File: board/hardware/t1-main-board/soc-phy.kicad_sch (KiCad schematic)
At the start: 1 part, among them U1301 RK3566

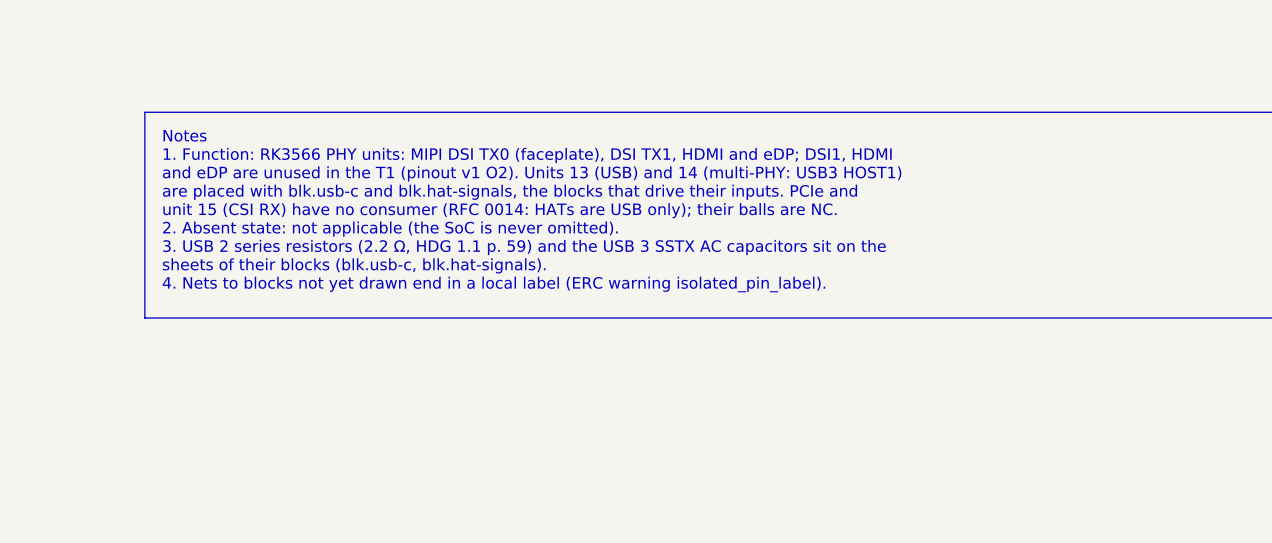
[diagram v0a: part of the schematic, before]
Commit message: Board: capture blk.maskrom
Power + Vol- at a cold power-on pull eMMC D0 low inside the TPS3808G01
boot window (BOM v1 lines 35, 78, 97, 98; sim/maskrom): SENSE 280k/100k,
CT 390 nF, WINDOW_N with its pad, SN74LVC1G57 and SN74LVC1G58 on
vcca1v8_pmu, BAT54 from PWRON_N, DMG1012T through 1 kΩ to EMMC_D0.
Every block in use now has its sheet; the README states the remaining
single-pin nets.

Co-Authored-By: Claude Opus 5.5 <noreply@anthropic.com>
Claude-Session: https://claude.ai/code/session_01Ei262h3TpgY9vyfNLMi5Mn
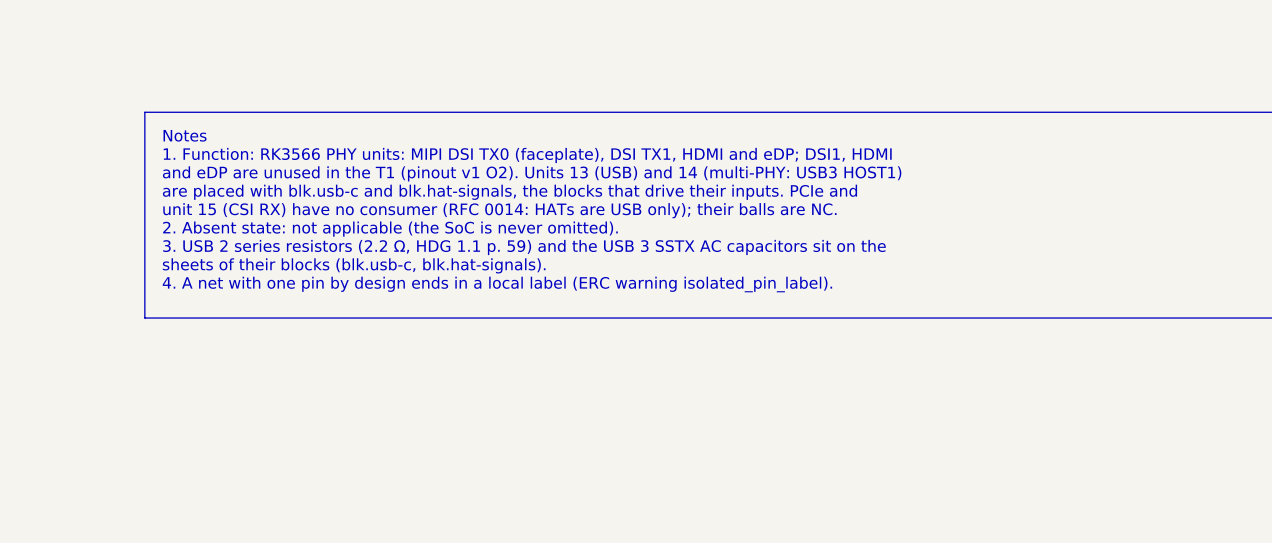
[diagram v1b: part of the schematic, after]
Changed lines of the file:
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@@
 (no_connect (at 76.2 138.43))
 (no_connect (at 76.2 140.97))
-(text_box "Notes\n1. Function: RK3566 PHY units: MIPI DSI TX0 (faceplate), DSI TX1, HDMI and eDP; DSI1, HDMI\n   and eDP are unused in the T1 (pinout v1 O2). Units 13 (USB) and 14 (multi-PHY: USB3 HOST1)\n   are placed with blk.usb-c and blk.hat-signals, the blocks that drive their inputs. PCIe and\n   unit 15 (CSI RX) have no consumer (RFC 0014: HATs are USB only); their balls are NC.\n2. Absent state: not applicable (the SoC is never omitted).\n3. USB 2 series resistors (2.2 Ω, HDG 1.1 p. 59) and the USB 3 SSTX AC capacitors sit on the\n   sheets of their blocks (blk.usb-c, blk.hat-signals).\n4. Nets to blocks not yet drawn end in a local label (ERC warning isolated_pin_label)." (exclude_from_sim no) (at 275.59 226.06 0) (size 129.54 22.86) (margins 1.905 1.905 1.905 1.905) (stroke (width 0) (type default)) (fill (type none)) (effects (font (size 1.27 1.27)) (justify left top)))
+(text_box "Notes\n1. Function: RK3566 PHY units: MIPI DSI TX0 (faceplate), DSI TX1, HDMI and eDP; DSI1, HDMI\n   and eDP are unused in the T1 (pinout v1 O2). Units 13 (USB) and 14 (multi-PHY: USB3 HOST1)\n   are placed with blk.usb-c and blk.hat-signals, the blocks that drive their inputs. PCIe and\n   unit 15 (CSI RX) have no consumer (RFC 0014: HATs are USB only); their balls are NC.\n2. Absent state: not applicable (the SoC is never omitted).\n3. USB 2 series resistors (2.2 Ω, HDG 1.1 p. 59) and the USB 3 SSTX AC capacitors sit on the\n   sheets of their blocks (blk.usb-c, blk.hat-signals).\n4. A net with one pin by design ends in a local label (ERC warning isolated_pin_label)." (exclude_from_sim no) (at 275.59 226.06 0) (size 129.54 22.86) (margins 1.905 1.905 1.905 1.905) (stroke (width 0) (type default)) (fill (type none)) (effects (font (size 1.27 1.27)) (justify left top)))
 (label "HAT_USB3_DM" (at 44.45 41.91 180) (effects (font (size 1.27 1.27)) (justify right bottom)))
 (label "HAT_USB3_DP" (at 44.45 44.45 180) (effects (font (size 1.27 1.27)) (justify right bottom)))

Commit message: Board on libs v0.2.0: lower-case kebab vendor keys (HL-13)
The libs submodule moves to v0.2.0 (5f24483). Every library nickname in
the generator, the placement tool and the floorplan study follows the
key table (Texas_Instruments -> texas-instruments, OpenDAP_Device ->
opendap-generic, Rockchip and Rockchip_PMIC -> rockchip, ...); the
library tables are written from the files. Schematic and board
regenerated.

Checks: ERC 0 errors (warnings unchanged); DRC 0 errors, 605 warnings,
the same counts by type, schematic parity 0; every placement identical;
craft Q1 met; pcb tests pass; STEP export resolves every libs 3D model
(the 27 parts without a model are KiCad stock lands that have none).

Co-Authored-By: Claude Opus 5.5 <noreply@anthropic.com>
Claude-Session: https://claude.ai/code/session_01Ei262h3TpgY9vyfNLMi5Mn
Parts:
- U1301: footprint Rockchip:Rockchip_FCCSP-565L_15.5x14.4mm_P0.4mm_P0.65mm_Ball0.25mm_Pad0.25mm_NSMD -> rockchip:Rockchip_FCCSP-565L_15.5x14.4mm_P0.4mm_P0.65mm_Ball0.25mm_Pad0.25mm_NSMD; symbol Rockchip:RK3566 -> rockchip:RK3566
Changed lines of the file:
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@@
 (paper "A3")
 (title_block (title "SoC: USB, PCIe, MIPI, HDMI and eDP PHYs") (date "2026-10-25") (rev "A") (company "The OpenDAP Project") (comment 1 "blk.soc-phy") (comment 2 "RK3566 PHY units: USB 2.0 and USB 3, multi-PHY, MIPI CSI RX, MIPI DSI TX0 and TX1, HDMI and eDP"))
-(symbol (lib_id "Rockchip:RK3566") (at 87.63 57.15 0) (unit 13) (body_style 1) (exclude_from_sim no) (in_bom yes) (on_board yes) (dnp no)
+(symbol (lib_id "rockchip:RK3566") (at 87.63 57.15 0) (unit 13) (body_style 1) (exclude_from_sim no) (in_bom yes) (on_board yes) (dnp no)
   (property "Reference" "U1301" (at 53.34 35.56 0) (effects (font (size 1.27 1.27)) (justify left)))
   (property "Value" "RK3566" (at 53.34 33.02 0) (effects (font (size 1.27 1.27)) (justify left)))
-  (property "Footprint" "Rockchip:Rockchip_FCCSP-565L_15.5x14.4mm_P0.4mm_P0.65mm_Ball0.25mm_Pad0.25mm_NSMD" (at 87.63 57.15 0) (effects (font (size 1.27 1.27))) (hide yes))
+  (property "Footprint" "rockchip:Rockchip_FCCSP-565L_15.5x14.4mm_P0.4mm_P0.65mm_Ball0.25mm_Pad0.25mm_NSMD" (at 87.63 57.15 0) (effects (font (size 1.27 1.27))) (hide yes))
   (property "Datasheet" "https://dl.xkwy2018.com/downloads/RK3568/Rockchip-RK3566-Datasheet-V1.1-20210305.pdf" (at 87.63 57.15 0) (effects (font (size 1.27 1.27))) (hide yes))
   (property "Description" "Quad-core Arm Cortex-A55 application processor, LPDDR4X/DDR4 32-bit, eMMC 5.1, FCCSP565L 15.5 x 14.4 mm" (at 87.63 57.15 0) (effects (font (size 1.27 1.27))) (hide yes))
@@
 (wire (pts (xy 128.27 41.91) (xy 130.81 41.91)) (stroke (width 0) (type default)))
 (wire (pts (xy 128.27 44.45) (xy 130.81 44.45)) (stroke (width 0) (type default)))
-(symbol (lib_id "Rockchip:RK3566") (at 191.77 46.99 0) (unit 14) (body_style 1) (exclude_from_sim no) (in_bom yes) (on_board yes) (dnp no)
+(symbol (lib_id "rockchip:RK3566") (at 191.77 46.99 0) (unit 14) (body_style 1) (exclude_from_sim no) (in_bom yes) (on_board yes) (dnp no)
   (property "Reference" "U1301" (at 162.56 35.56 0) (effects (font (size 1.27 1.27)) (justify left)))
   (property "Value" "RK3566" (at 162.56 33.02 0) (effects (font (size 1.27 1.27)) (justify left)))
-  (property "Footprint" "Rockchip:Rockchip_FCCSP-565L_15.5x14.4mm_P0.4mm_P0.65mm_Ball0.25mm_Pad0.25mm_NSMD" (at 191.77 46.99 0) (effects (font (size 1.27 1.27))) (hide yes))
+  (property "Footprint" "rockchip:Rockchip_FCCSP-565L_15.5x14.4mm_P0.4mm_P0.65mm_Ball0.25mm_Pad0.25mm_NSMD" (at 191.77 46.99 0) (effects (font (size 1.27 1.27))) (hide yes))
   (property "Datasheet" "https://dl.xkwy2018.com/downloads/RK3568/Rockchip-RK3566-Datasheet-V1.1-20210305.pdf" (at 191.77 46.99 0) (effects (font (size 1.27 1.27))) (hide yes))
   (property "Description" "Quad-core Arm Cortex-A55 application processor, LPDDR4X/DDR4 32-bit, eMMC 5.1, FCCSP565L 15.5 x 14.4 mm" (at 191.77 46.99 0) (effects (font (size 1.27 1.27))) (hide yes))
@@
 (no_connect (at 227.33 46.99))
 (no_connect (at 227.33 49.53))
-(symbol (lib_id "Rockchip:RK3566") (at 255.27 57.15 0) (unit 15) (body_style 1) (exclude_from_sim no) (in_bom yes) (on_board yes) (dnp no)
+(symbol (lib_id "rockchip:RK3566") (at 255.27 57.15 0) (unit 15) (body_style 1) (exclude_from_sim no) (in_bom yes) (on_board yes) (dnp no)
   (property "Reference" "U1301" (at 241.3 35.56 0) (effects (font (size 1.27 1.27)) (justify left)))
   (property "Value" "RK3566" (at 241.3 33.02 0) (effects (font (size 1.27 1.27)) (justify left)))
-  (property "Footprint" "Rockchip:Rockchip_FCCSP-565L_15.5x14.4mm_P0.4mm_P0.65mm_Ball0.25mm_Pad0.25mm_NSMD" (at 255.27 57.15 0) (effects (font (size 1.27 1.27))) (hide yes))
+  (property "Footprint" "rockchip:Rockchip_FCCSP-565L_15.5x14.4mm_P0.4mm_P0.65mm_Ball0.25mm_Pad0.25mm_NSMD" (at 255.27 57.15 0) (effects (font (size 1.27 1.27))) (hide yes))
   (property "Datasheet" "https://dl.xkwy2018.com/downloads/RK3568/Rockchip-RK3566-Datasheet-V1.1-20210305.pdf" (at 255.27 57.15 0) (effects (font (size 1.27 1.27))) (hide yes))
   (property "Description" "Quad-core Arm Cortex-A55 application processor, LPDDR4X/DDR4 32-bit, eMMC 5.1, FCCSP565L 15.5 x 14.4 mm" (at 255.27 57.15 0) (effects (font (size 1.27 1.27))) (hide yes))
@@
 (no_connect (at 234.95 67.31))
 (no_connect (at 234.95 69.85))
-(symbol (lib_id "Rockchip:RK3566") (at 300.99 54.61 0) (unit 16) (body_style 1) (exclude_from_sim no) (in_bom yes) (on_board yes) (dnp no)
+(symbol (lib_id "rockchip:RK3566") (at 300.99 54.61 0) (unit 16) (body_style 1) (exclude_from_sim no) (in_bom yes) (on_board yes) (dnp no)
   (property "Reference" "U1301" (at 276.86 35.56 0) (effects (font (size 1.27 1.27)) (justify left)))
   (property "Value" "RK3566" (at 276.86 33.02 0) (effects (font (size 1.27 1.27)) (justify left)))
-  (property "Footprint" "Rockchip:Rockchip_FCCSP-565L_15.5x14.4mm_P0.4mm_P0.65mm_Ball0.25mm_Pad0.25mm_NSMD" (at 300.99 54.61 0) (effects (font (size 1.27 1.27))) (hide yes))
+  (property "Footprint" "rockchip:Rockchip_FCCSP-565L_15.5x14.4mm_P0.4mm_P0.65mm_Ball0.25mm_Pad0.25mm_NSMD" (at 300.99 54.61 0) (effects (font (size 1.27 1.27))) (hide yes))
   (property "Datasheet" "https://dl.xkwy2018.com/downloads/RK3568/Rockchip-RK3566-Datasheet-V1.1-20210305.pdf" (at 300.99 54.61 0) (effects (font (size 1.27 1.27))) (hide yes))
   (property "Description" "Quad-core Arm Cortex-A55 application processor, LPDDR4X/DDR4 32-bit, eMMC 5.1, FCCSP565L 15.5 x 14.4 mm" (at 300.99 54.61 0) (effects (font (size 1.27 1.27))) (hide yes))
@@
 (wire (pts (xy 331.47 62.23) (xy 334.01 62.23)) (stroke (width 0) (type default)))
 (wire (pts (xy 331.47 64.77) (xy 334.01 64.77)) (stroke (width 0) (type default)))
-(symbol (lib_id "Rockchip:RK3566") (at 370.84 54.61 0) (unit 17) (body_style 1) (exclude_from_sim no) (in_bom yes) (on_board yes) (dnp no)
+(symbol (lib_id "rockchip:RK3566") (at 370.84 54.61 0) (unit 17) (body_style 1) (exclude_from_sim no) (in_bom yes) (on_board yes) (dnp no)
   (property "Reference" "U1301" (at 356.87 35.56 0) (effects (font (size 1.27 1.27)) (justify left)))
   (property "Value" "RK3566" (at 356.87 33.02 0) (effects (font (size 1.27 1.27)) (justify left)))
-  (property "Footprint" "Rockchip:Rockchip_FCCSP-565L_15.5x14.4mm_P0.4mm_P0.65mm_Ball0.25mm_Pad0.25mm_NSMD" (at 370.84 54.61 0) (effects (font (size 1.27 1.27))) (hide yes))
+  (property "Footprint" "rockchip:Rockchip_FCCSP-565L_15.5x14.4mm_P0.4mm_P0.65mm_Ball0.25mm_Pad0.25mm_NSMD" (at 370.84 54.61 0) (effects (font (size 1.27 1.27))) (hide yes))
   (property "Datasheet" "https://dl.xkwy2018.com/downloads/RK3568/Rockchip-RK3566-Datasheet-V1.1-20210305.pdf" (at 370.84 54.61 0) (effects (font (size 1.27 1.27))) (hide yes))
   (property "Description" "Quad-core Arm Cortex-A55 application processor, LPDDR4X/DDR4 32-bit, eMMC 5.1, FCCSP565L 15.5 x 14.4 mm" (at 370.84 54.61 0) (effects (font (size 1.27 1.27))) (hide yes))
@@
 (no_connect (at 391.16 62.23))
 (no_connect (at 391.16 64.77))
-(symbol (lib_id "Rockchip:RK3566") (at 50.8 118.11 0) (unit 18) (body_style 1) (exclude_from_sim no) (in_bom yes) (on_board yes) (dnp no)
+(symbol (lib_id "rockchip:RK3566") (at 50.8 118.11 0) (unit 18) (body_style 1) (exclude_from_sim no) (in_bom yes) (on_board yes) (dnp no)
   (property "Reference" "U1301" (at 31.75 88.9 0) (effects (font (size 1.27 1.27)) (justify left)))
   (property "Value" "RK3566" (at 31.75 86.36 0) (effects (font (size 1.27 1.27)) (justify left)))
-  (property "Footprint" "Rockchip:Rockchip_FCCSP-565L_15.5x14.4mm_P0.4mm_P0.65mm_Ball0.25mm_Pad0.25mm_NSMD" (at 50.8 118.11 0) (effects (font (size 1.27 1.27))) (hide yes))
+  (property "Footprint" "rockchip:Rockchip_FCCSP-565L_15.5x14.4mm_P0.4mm_P0.65mm_Ball0.25mm_Pad0.25mm_NSMD" (at 50.8 118.11 0) (effects (font (size 1.27 1.27))) (hide yes))
   (property "Datasheet" "https://dl.xkwy2018.com/downloads/RK3568/Rockchip-RK3566-Datasheet-V1.1-20210305.pdf" (at 50.8 118.11 0) (effects (font (size 1.27 1.27))) (hide yes))
   (property "Description" "Quad-core Arm Cortex-A55 application processor, LPDDR4X/DDR4 32-bit, eMMC 5.1, FCCSP565L 15.5 x 14.4 mm" (at 50.8 118.11 0) (effects (font (size 1.27 1.27))) (hide yes))

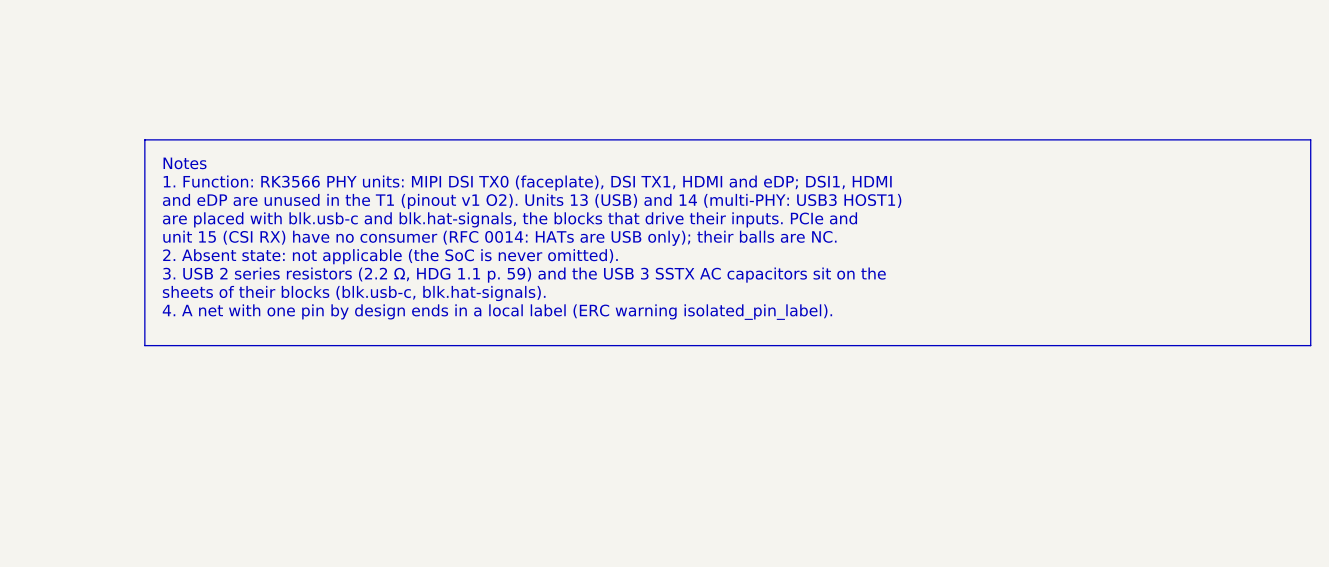
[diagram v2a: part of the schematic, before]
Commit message: Board: pre-PCB schematic items closed with datasheets (BOM v1.22)
Display INA236 to 0x49 (INA236B, A0 = VS): no A0 = SDA strap, so the
address no longer depends on the host's I2C hold time. The 18 WSL
shunts and links on Vishay's doc 30100 lands. 24 MHz crystal NDK
NX3225GA (CL 8 pF) with 2 x 10 pF. Backlight inductor Coilcraft
XFL3012-223MEC on its published land (no placeholder left). Action
button PTS815 G code on the side-button land. Cover-detect leakage,
TPS3808 spread, RP2354A supply pins and the USB series scheme closed
without change. Placement v1.9: 100.2 % need, factor 1.64, DRC 0
errors; power tree v0.12; PCB-Z-08 and CB-08 strip values.

Co-Authored-By: Claude Opus 5.5 <noreply@anthropic.com>
Claude-Session: https://claude.ai/code/session_013P6pW9LdyEMFishwCcZGUr
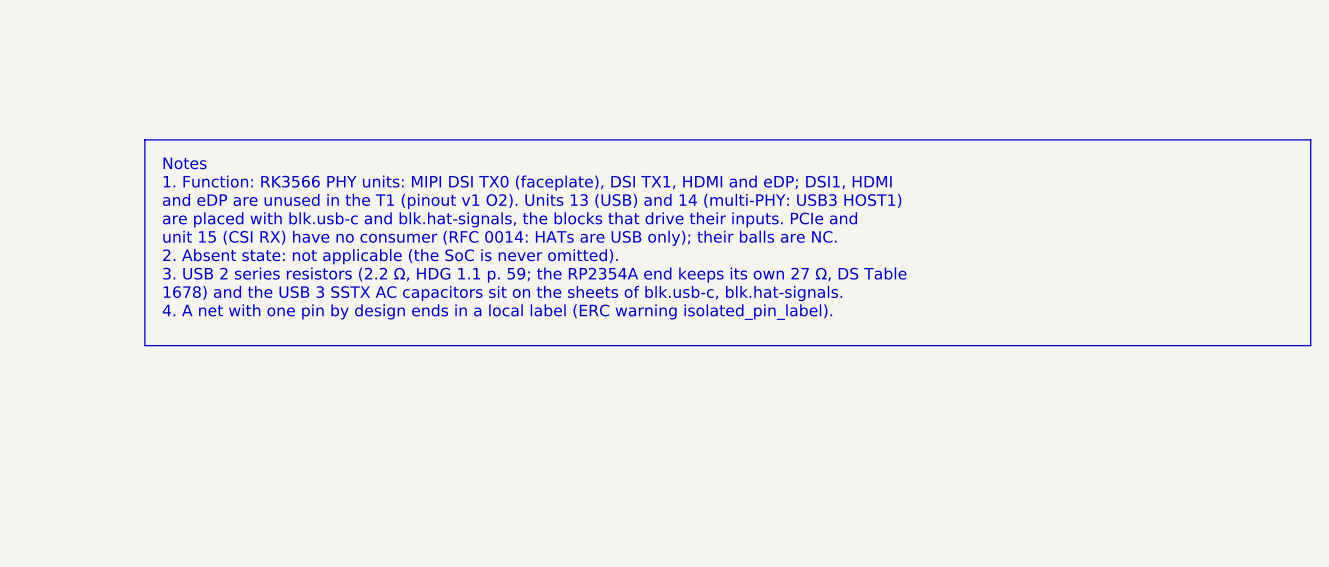
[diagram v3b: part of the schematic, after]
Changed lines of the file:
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@@
 (no_connect (at 76.2 138.43))
 (no_connect (at 76.2 140.97))
-(text_box "Notes\n1. Function: RK3566 PHY units: MIPI DSI TX0 (faceplate), DSI TX1, HDMI and eDP; DSI1, HDMI\n   and eDP are unused in the T1 (pinout v1 O2). Units 13 (USB) and 14 (multi-PHY: USB3 HOST1)\n   are placed with blk.usb-c and blk.hat-signals, the blocks that drive their inputs. PCIe and\n   unit 15 (CSI RX) have no consumer (RFC 0014: HATs are USB only); their balls are NC.\n2. Absent state: not applicable (the SoC is never omitted).\n3. USB 2 series resistors (2.2 Ω, HDG 1.1 p. 59) and the USB 3 SSTX AC capacitors sit on the\n   sheets of their blocks (blk.usb-c, blk.hat-signals).\n4. A net with one pin by design ends in a local label (ERC warning isolated_pin_label)." (exclude_from_sim no) (at 275.59 226.06 0) (size 129.54 22.86) (margins 1.905 1.905 1.905 1.905) (stroke (width 0) (type default)) (fill (type none)) (effects (font (size 1.27 1.27)) (justify left top)))
+(text_box "Notes\n1. Function: RK3566 PHY units: MIPI DSI TX0 (faceplate), DSI TX1, HDMI and eDP; DSI1, HDMI\n   and eDP are unused in the T1 (pinout v1 O2). Units 13 (USB) and 14 (multi-PHY: USB3 HOST1)\n   are placed with blk.usb-c and blk.hat-signals, the blocks that drive their inputs. PCIe and\n   unit 15 (CSI RX) have no consumer (RFC 0014: HATs are USB only); their balls are NC.\n2. Absent state: not applicable (the SoC is never omitted).\n3. USB 2 series resistors (2.2 Ω, HDG 1.1 p. 59; the RP2354A end keeps its own 27 Ω, DS Table\n   1678) and the USB 3 SSTX AC capacitors sit on the sheets of blk.usb-c, blk.hat-signals.\n4. A net with one pin by design ends in a local label (ERC warning isolated_pin_label)." (exclude_from_sim no) (at 275.59 226.06 0) (size 129.54 22.86) (margins 1.905 1.905 1.905 1.905) (stroke (width 0) (type default)) (fill (type none)) (effects (font (size 1.27 1.27)) (justify left top)))
 (label "HAT_USB3_DM" (at 44.45 41.91 180) (effects (font (size 1.27 1.27)) (justify right bottom)))
 (label "HAT_USB3_DP" (at 44.45 44.45 180) (effects (font (size 1.27 1.27)) (justify right bottom)))
